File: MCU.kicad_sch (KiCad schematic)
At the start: 11 parts, among them J1 Conn_ARM_JTAG_SWD_10, SW1 SW_SPDT, U2 M95P32-IXMNT_E, U3 STM32H725ZGT6, Y1 ABS05W-32.768KHZ-D-2-T, Y2 ECS-80-8-30Q-VY-TR

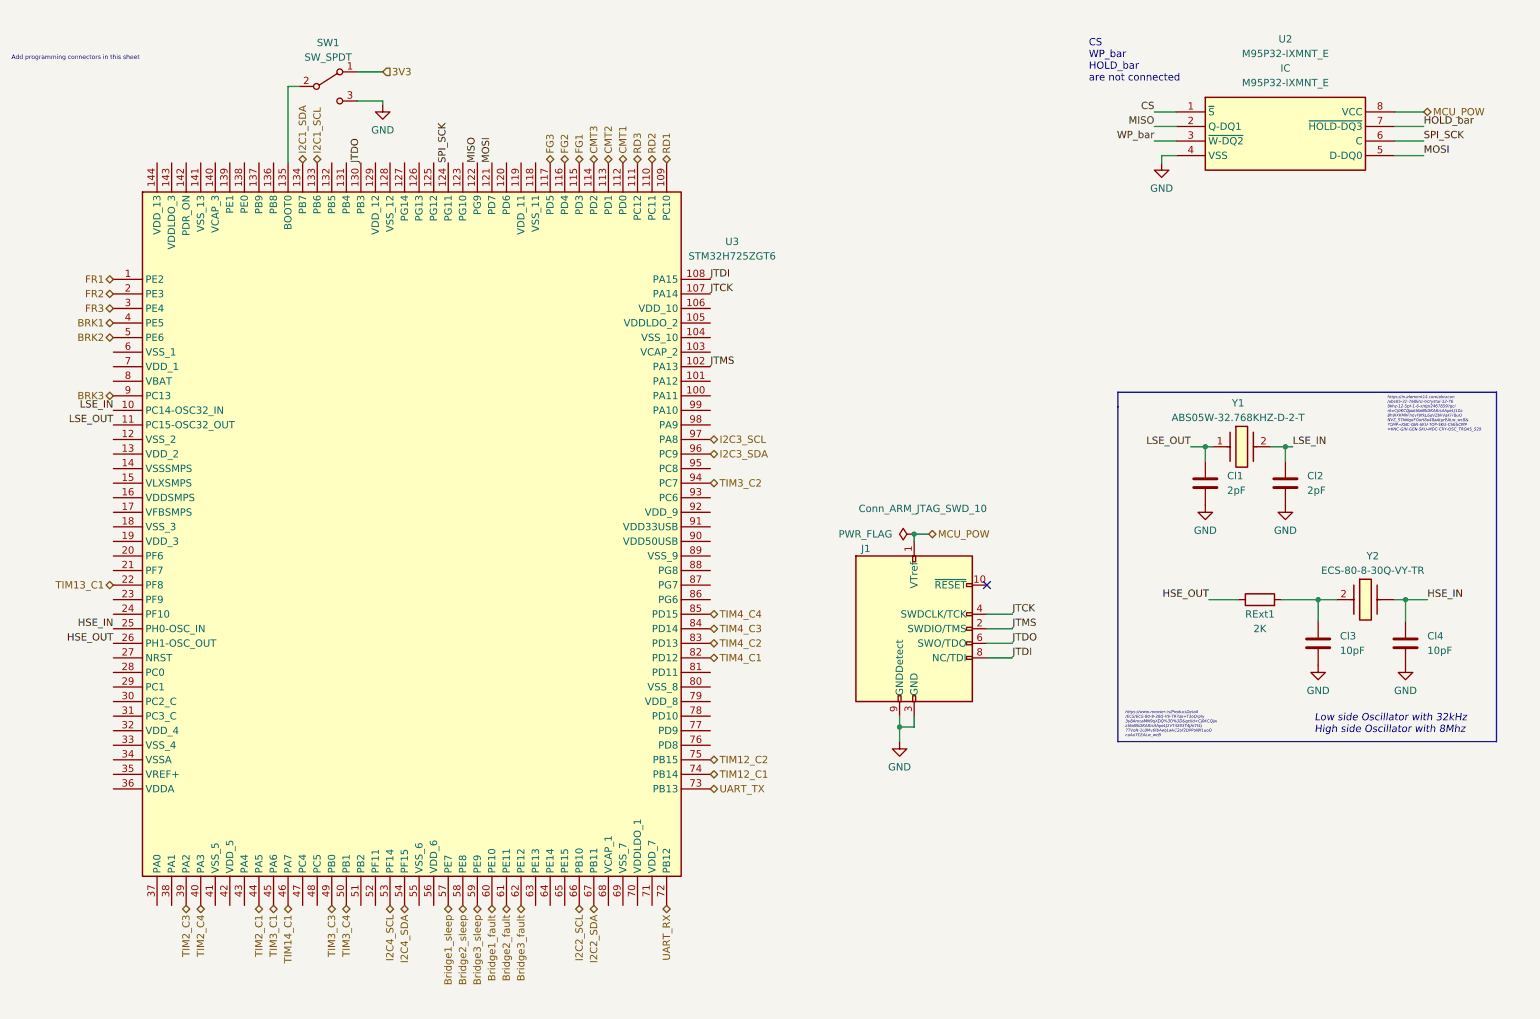
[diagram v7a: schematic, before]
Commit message: Page settings changed. Added some testpoints. Some comments are made.
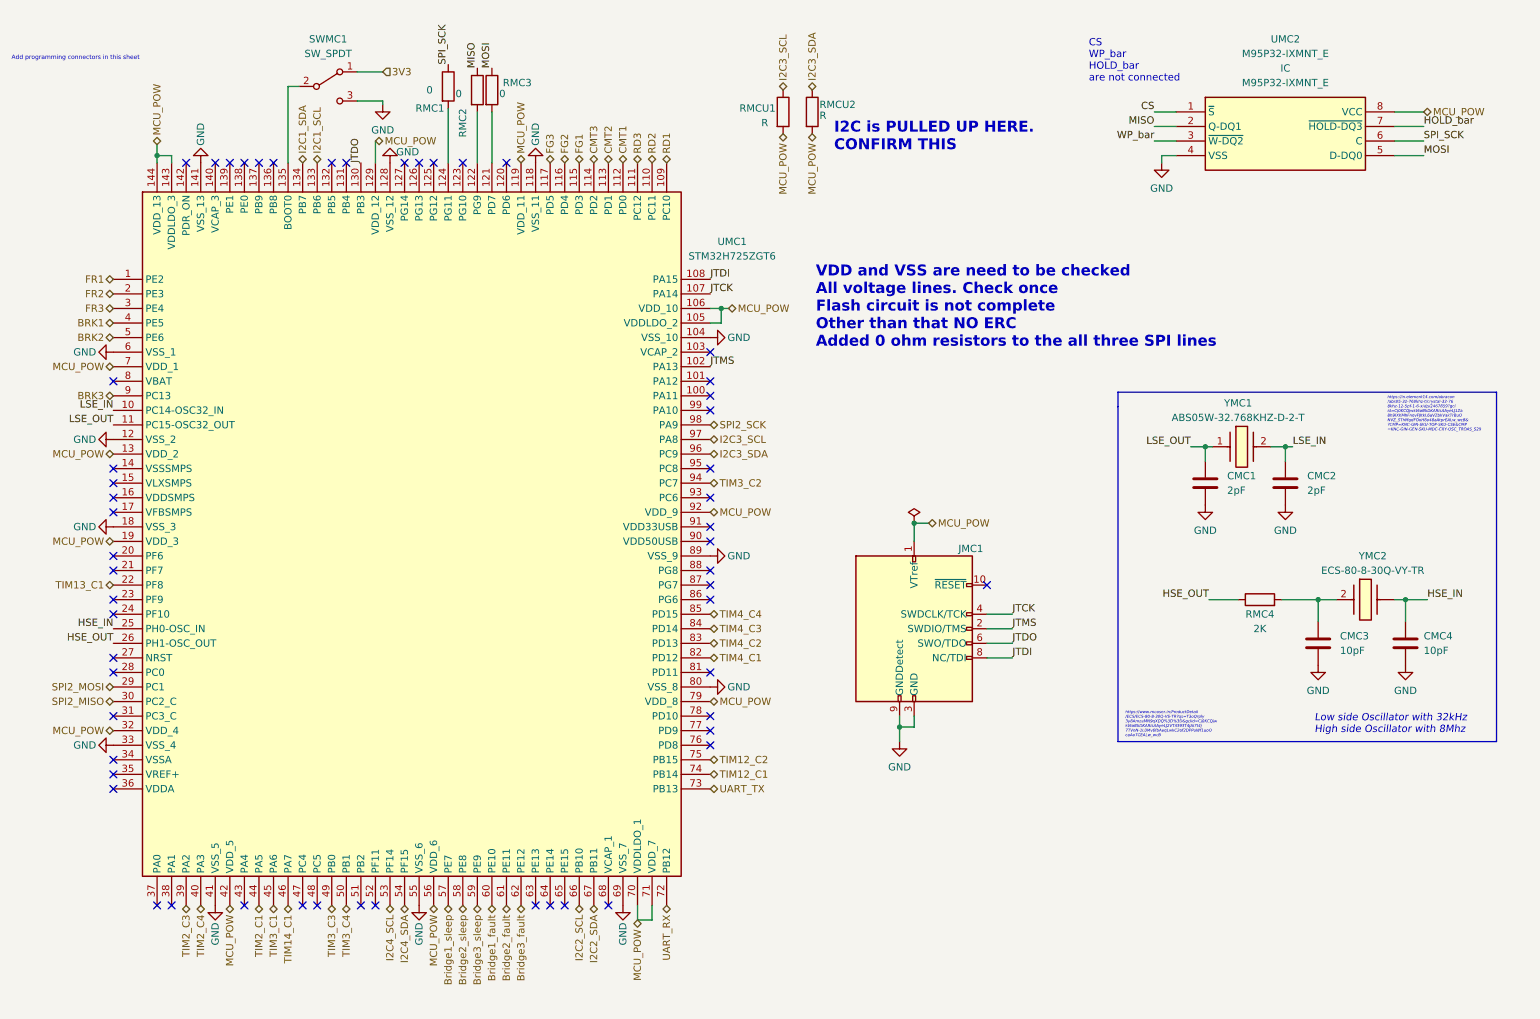
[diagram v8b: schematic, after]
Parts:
- added RMC1, RMC2, RMC3: 0, symbol Device:R
- added RMCU1, RMCU2: R, symbol Device:R
- renumbered Cl1 to CMC1, Cl2 to CMC2, Cl3 to CMC3, Cl4 to CMC4, J1 to JMC1, RExt1 to RMC4, SW1 to SWMC1, U3 to UMC1, U2 to UMC2, Y1 to YMC1, Y2 to YMC2
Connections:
- net GND: now also UMC1.104 (VSS_10), UMC1.118 (VSS_11), UMC1.12 (VSS_2), UMC1.128 (VSS_12), UMC1.141 (VSS_13), UMC1.18 (VSS_3), UMC1.33 (VSS_4), UMC1.41 (VSS_5), UMC1.55 (VSS_6), UMC1.6 (VSS_1), UMC1.69 (VSS_7), UMC1.80 (VSS_8), UMC1.89 (VSS_9)
- net I2C3_SCL: now also RMCU1.1
- net I2C3_SDA: now also RMCU2.1
- net MCU_POW: now also UMC1.105 (VDDLDO_2), UMC1.106 (VDD_10), UMC1.119 (VDD_11), UMC1.129 (VDD_12), UMC1.13 (VDD_2), UMC1.143 (VDDLDO_3), UMC1.144 (VDD_13), UMC1.19 (VDD_3), UMC1.32 (VDD_4), UMC1.42 (VDD_5), UMC1.56 (VDD_6), UMC1.7 (VDD_1), UMC1.70 (VDDLDO_1), UMC1.71 (VDD_7), UMC1.79 (VDD_8), UMC1.92 (VDD_9), RMCU1.2, RMCU2.2
- net MISO: now also RMC2.1; no longer UMC1.122 (PG9)
- net MOSI: now also RMC3.1; no longer UMC1.121 (PD7)
- net SPI_SCK: now also RMC1.1; no longer UMC1.124 (PG11)
- net SPI2_MOSI: now reaches UMC1.29 (PC1)
- net SPI2_MISO: now reaches UMC1.30 (PC2_C)
- net SPI2_SCK: now reaches UMC1.98 (PA9)
- new net: RMC1.2, UMC1.124 (PG11)
- new net: RMC3.2, UMC1.121 (PD7)
- new net: RMC2.2, UMC1.122 (PG9)
- no-connect marks 1 -> 55
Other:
- note added: "I2C is PULLED UP HERE. CONFIRM THIS"
- note added: "VDD and VSS are need to be checked All voltage lines. Check once Flash circuit is not complete Other than that NO ERC Added 0 ohm resistors to the all three SPI lines"
